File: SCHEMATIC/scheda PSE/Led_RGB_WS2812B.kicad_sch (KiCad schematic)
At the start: 16 parts

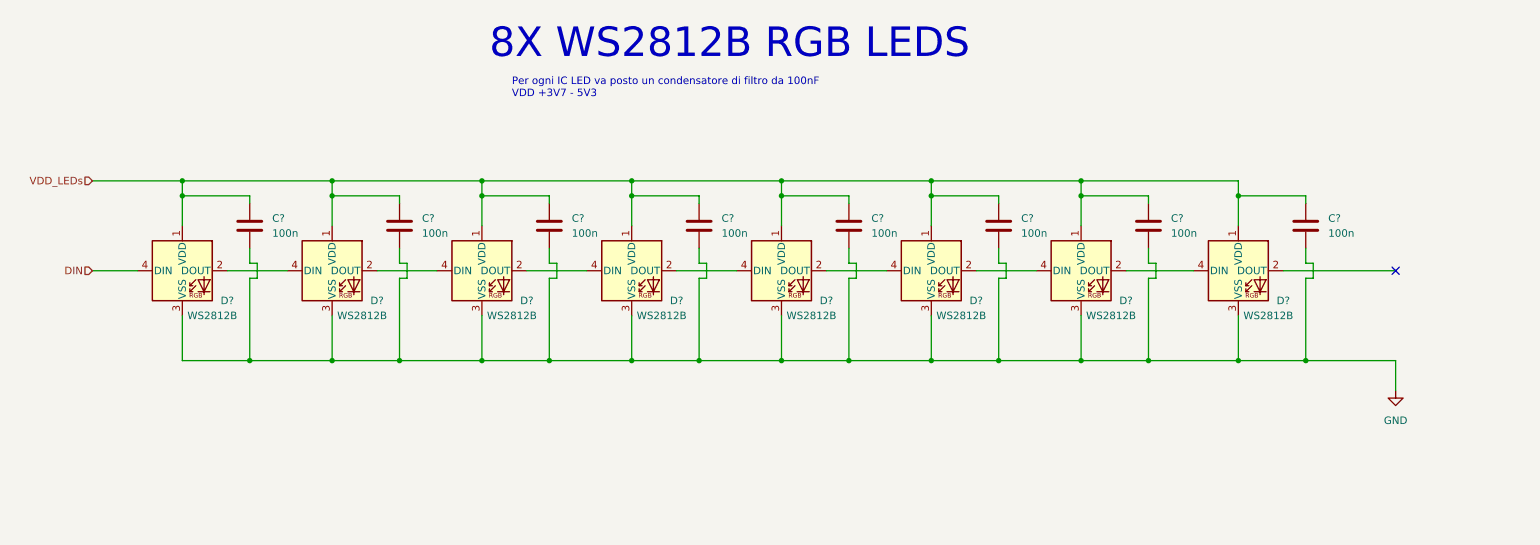
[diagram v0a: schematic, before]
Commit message: Sistemato tutto lo schematico con fogli gerarchici
Sistemato lo schematico, ordinato tutti i componenti nei vari fogli gerarchici.
aggiunto ldo e sistemato il buck converter. aggiunti anche i terminali a vite per le connessioni esterne
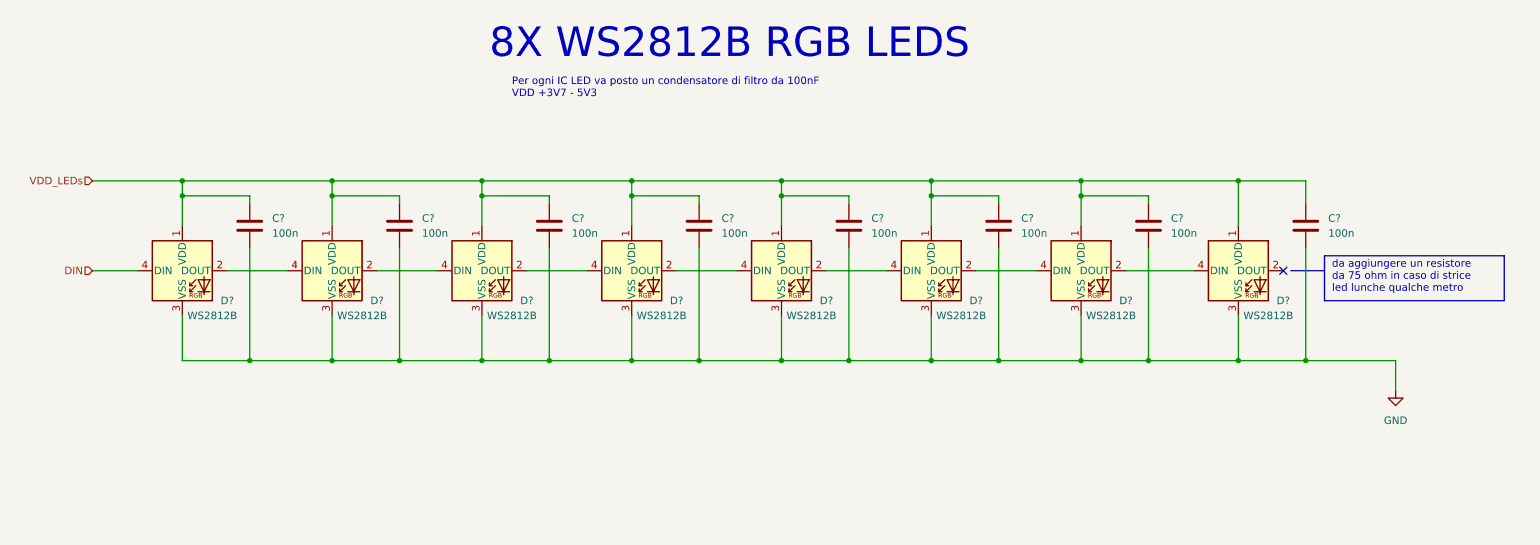
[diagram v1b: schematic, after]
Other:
- note added: "da aggiungere un resistore da 75 ohm in caso di strice led lunche qualche metro"
- title: (none) -> Scheda PSE RP2040

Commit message: sistemato tutto, e aggiunti i footprint da modificare
sistemato tutto, aggiunto e modificato i footprint.
Manca solo aggiungere i restanti footprint (praticamente solo dei componenti comuni)
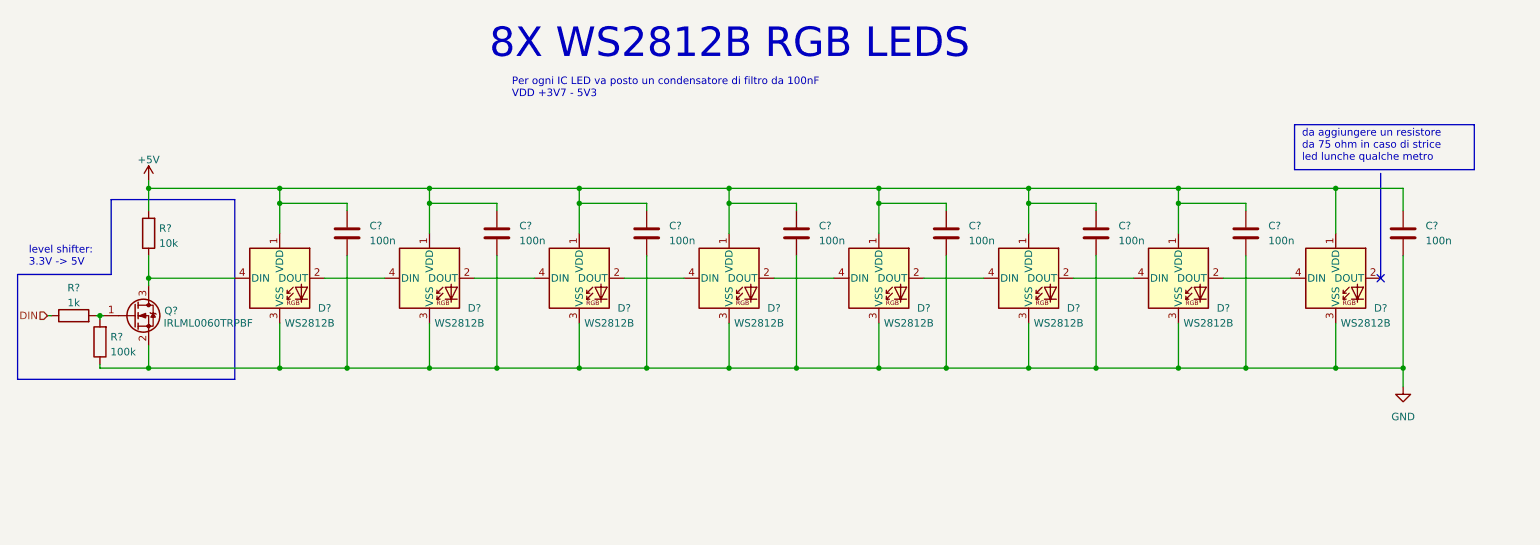
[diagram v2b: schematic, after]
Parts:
- added Q?: IRLML0060TRPBF, Package_TO_SOT_SMD:SOT-23, symbol Transistor_FET:IRLML2060
- added R?: 100k, symbol Device:R
- added R?: 10k, symbol Device:R
- added R?: 1k, symbol Device:R
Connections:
- net DIN: now also R?.1; no longer D?.4 (DIN)
- net GND: now also Q?.2 (S), R?.1
- net VDD_LEDs renamed +5V
- net +5V: now also R?.2
- new net: Q?.1 (G), R?.2, R?.2
- new net: D?.4 (DIN), Q?.3 (D), R?.1
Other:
- note added: "level shifter: 3.3V -> 5V"
- moved on the sheet: C?, D?

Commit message: Aggiunti QUASI tutti i footprint
aggiunti quasi tutti i footprint dei componenti
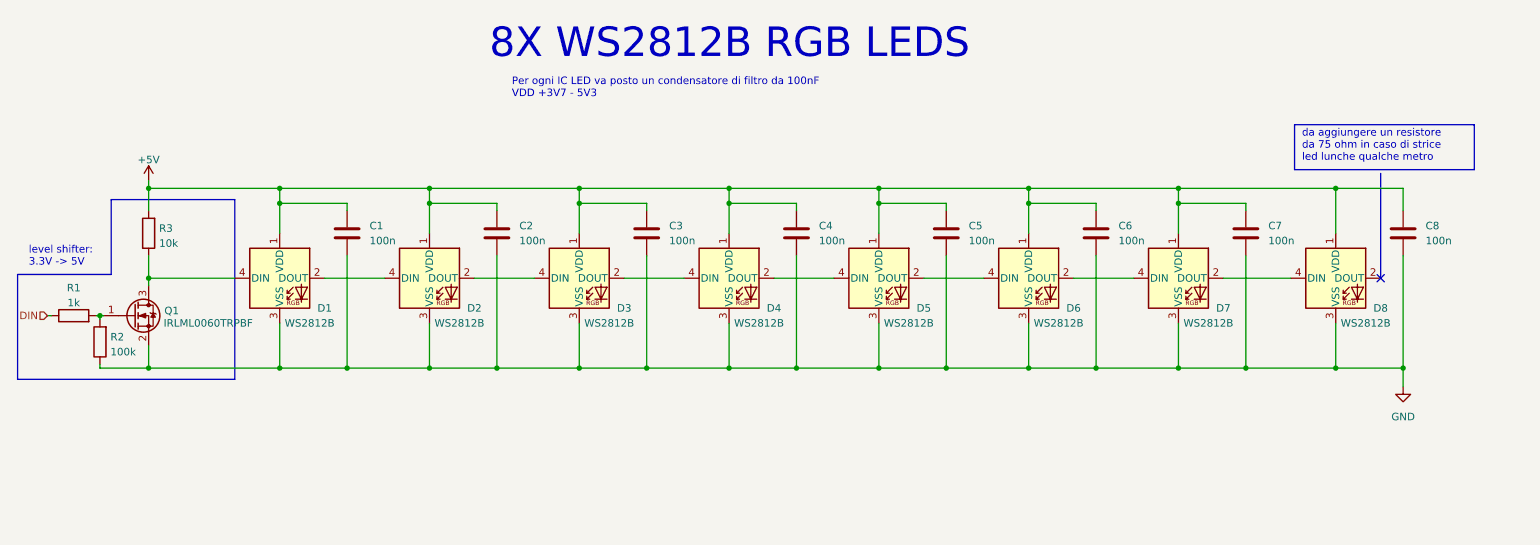
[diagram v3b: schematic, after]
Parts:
- C1, C2, C3, C4, C5, C6, C7, C8: renamed from C?; footprint (none) -> Capacitor_SMD:C_0603_1608Metric
- R1, R2, R3: renamed from R?; footprint (none) -> Resistor_SMD:R_0603_1608Metric
- gave numbers to parts that had none: 9

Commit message: Aggiunte tutte le cose richieste dal prof
Aggiunte tutte le cose richieste dal prof:
wifi
servo
uscita led
MANCA DA METERE IL SOLDER MASK SUI PAD NON USATI DEL GPS
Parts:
- added J1: WS2812B, Connector_JST:JST_XH_B3B-XH-A_1x03_P2.50mm_Vertical, symbol Connector_Generic:Conn_01x03
- added JP1: EXT_LEDs, Connector_PinHeader_2.54mm:PinHeader_1x02_P2.54mm_Vertical, symbol Jumper:Jumper_2_Open
- R3: value 10k -> 1k
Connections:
- net +5V: now also J1.2 (Pin_2)
- net DIN: now also Q1.3 (D), R3.1, J1.1 (Pin_1), JP1.1 (A)
- net GND: now also J1.3 (Pin_3)
- new net: D1.4 (DIN), JP1.2 (B)
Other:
- note added: "Connettore per striscia led esterna"
- note added: "da aggiungere un resistore da 75 ohm in caso di strice led lunghe qualche metro"
- note removed: "da aggiungere un resistore da 75 ohm in caso di strice led lunche qualche metro"
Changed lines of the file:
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@@
   (title_block
     (title "Scheda PSE RP2040")
-    (date "2023-03-29")
+    (date "2023-04-04")
     (rev "1.0")
     (comment 1 "Filippo Castellan ")
@@
   (junction (at 199.39 86.36) (diameter 0) (color 0 0 0 0)
   )
+  (junction (at 50.165 99.06) (diameter 0) (color 0 0 0 0)
+  )
   (junction (at 173.99 114.3) (diameter 0) (color 0 0 0 0)
   )
@@
   )
   (junction (at 173.99 83.82) (diameter 0) (color 0 0 0 0)
-  )
-  (junction (at 50.165 99.06) (diameter 0) (color 0 0 0 0)
   )
   (junction (at 224.79 86.36) (diameter 0) (color 0 0 0 0)
@@
     (stroke (width 0) (type default) (color 0 0 0 0))
   )
+  (wire (pts (xy 52.705 99.06) (xy 50.165 99.06))
+    (stroke (width 0) (type default) (color 0 0 0 0))
+  )
   (wire (pts (xy 123.19 83.82) (xy 148.59 83.82))
     (stroke (width 0) (type default) (color 0 0 0 0))
@@
     (stroke (width 0) (type default) (color 0 0 0 0))
   )
+  (wire (pts (xy 43.18 128.905) (xy 43.18 132.08))
+    (stroke (width 0) (type default) (color 0 0 0 0))
+  )
   (wire (pts (xy 224.79 86.36) (xy 224.79 91.44))
     (stroke (width 0) (type default) (color 0 0 0 0))
@@
     (stroke (width 0) (type default) (color 0 0 0 0))
   )
-  (wire (pts (xy 50.165 99.06) (xy 50.165 95.25))
+  (wire (pts (xy 50.165 95.25) (xy 50.165 99.06))
     (stroke (width 0) (type default) (color 0 0 0 0))
   )
@@
     (stroke (width 0) (type default) (color 0 0 0 0))
   )
+  (wire (pts (xy 43.18 132.08) (xy 50.165 132.08))
+    (stroke (width 0) (type default) (color 0 0 0 0))
+  )
   (wire (pts (xy 83.82 114.3) (xy 97.79 114.3))
     (stroke (width 0) (type default) (color 0 0 0 0))
@@
     (stroke (width 0) (type default) (color 0 0 0 0))
   )
+  (wire (pts (xy 43.18 134.62) (xy 43.18 136.525))
+    (stroke (width 0) (type default) (color 0 0 0 0))
+  )
   (wire (pts (xy 109.22 114.3) (xy 123.19 114.3))
     (stroke (width 0) (type default) (color 0 0 0 0))
@@
     (stroke (width 0) (type default) (color 0 0 0 0))
   )
+  (wire (pts (xy 62.865 99.06) (xy 64.77 99.06))
+    (stroke (width 0) (type default) (color 0 0 0 0))
+  )
   (wire (pts (xy 224.79 83.82) (xy 251.46 83.82))
     (stroke (width 0) (type default) (color 0 0 0 0))
@@
     (stroke (width 0) (type default) (color 0 0 0 0))
   )
+  (wire (pts (xy 50.165 134.62) (xy 43.18 134.62))
+    (stroke (width 0) (type default) (color 0 0 0 0))
+  )
   (polyline (pts (xy 274.955 80.645) (xy 244.475 80.645))
     (stroke (width 0) (type default) (color 0 0 0 0))
@@
     (stroke (width 0) (type default) (color 0 0 0 0))
   )
+  (wire (pts (xy 45.085 129.54) (xy 50.165 129.54))
+    (stroke (width 0) (type default) (color 0 0 0 0))
+  )
   (wire (pts (xy 123.19 114.3) (xy 134.62 114.3))
     (stroke (width 0) (type default) (color 0 0 0 0))
@@
     (stroke (width 0) (type default) (color 0 0 0 0))
   )
-  (wire (pts (xy 64.77 99.06) (xy 50.165 99.06))
-    (stroke (width 0) (type default) (color 0 0 0 0))
-  )
   (wire (pts (xy 148.59 114.3) (xy 160.02 114.3))
     (stroke (width 0) (type default) (color 0 0 0 0))
@@
     (stroke (width 0) (type default) (color 0 0 0 0))
   )
+  (wire (pts (xy 224.79 114.3) (xy 224.79 106.68))
+    (stroke (width 0) (type default) (color 0 0 0 0))
+  )
+  (wire (pts (xy 41.91 113.665) (xy 41.91 114.3))
+    (stroke (width 0) (type default) (color 0 0 0 0))
+  )
   (wire (pts (xy 50.165 99.06) (xy 50.165 100.33))
-    (stroke (width 0) (type default) (color 0 0 0 0))
-  )
-  (wire (pts (xy 224.79 114.3) (xy 224.79 106.68))
-    (stroke (width 0) (type default) (color 0 0 0 0))
-  )
-  (wire (pts (xy 41.91 113.665) (xy 41.91 114.3))
     (stroke (width 0) (type default) (color 0 0 0 0))
   )
@@
     (effects (font (size 1.27 1.27)) (justify left bottom))
   )
-  (text "da aggiungere un resistore\nda 75 ohm in caso di strice\nled lunche qualche metro"
+  (text "Connettore per striscia\nled esterna" (at 58.42 134.62 0)
+    (effects (font (size 1.27 1.27)) (justify left bottom))
+  )
+  (text "da aggiungere un resistore\nda 75 ohm in caso di strice\nled lunghe qualche metro"
     (at 245.745 79.375 0)
     (effects (font (size 1.27 1.27)) (justify left bottom))
@@
   (text "8X WS2812B RGB LEDS\n" (at 107.95 62.23 0)
     (effects (font (size 5 5)) (justify left bottom))
+  )
+  (label "DIN" (at 45.085 129.54 0)
+    (effects (font (size 1.27 1.27)) (justify left bottom))
+  )
+  (label "DIN" (at 50.165 99.06 0)
+    (effects (font (size 1.27 1.27)) (justify left bottom))
   )
   (hierarchical_label "DIN" (shape input) (at 33.02 105.41 180)
@@
   (symbol (lib_id "power:+5V") (at 50.165 82.55 0) (unit 1)
     (in_bom yes) (on_board yes) (fields_autoplaced)
-    (property "Reference" "#PWR01" (id 0) (at 50.165 86.36 0)
+    (property "Reference" "#PWR03" (id 0) (at 50.165 86.36 0)
       (effects (font (size 1.27 1.27)) hide)
     )
@@
   (symbol (lib_id "power:GND") (at 262.89 117.475 0) (unit 1)
     (in_bom yes) (on_board yes) (fields_autoplaced)
-    (property "Reference" "#PWR02" (id 0) (at 262.89 123.825 0)
+    (property "Reference" "#PWR04" (id 0) (at 262.89 123.825 0)
       (effects (font (size 1.27 1.27)) hide)
     )
@@
       (effects (font (size 1.27 1.27)) (justify right))
     )
-    (property "Value" "10k" (id 1) (at 51.943 93.1422 0)
+    (property "Value" "1k" (id 1) (at 51.943 93.1422 0)
       (effects (font (size 1.27 1.27)) (justify right))
     )
@@
     (pin "1")
     (pin "2")
+  )
+  (symbol (lib_id "power:GND") (at 43.18 136.525 0) (unit 1)
+    (in_bom yes) (on_board yes) (fields_autoplaced)
+    (property "Reference" "#PWR02" (id 0) (at 43.18 142.875 0)
+      (effects (font (size 1.27 1.27)) hide)
+    )
+    (property "Value" "GND" (id 1) (at 43.18 140.9684 0))
+    (property "Footprint" "" (id 2) (at 43.18 136.525 0)
+      (effects (font (size 1.27 1.27)) hide)
+    )
+    (property "Datasheet" "" (id 3) (at 43.18 136.525 0)
+      (effects (font (size 1.27 1.27)) hide)
+    )
+    (pin "1")
   )
   (symbol (lib_id "LED:WS2812B") (at 199.39 99.06 0) (unit 1)
@@
     (pin "4")
   )
+  (symbol (lib_id "Connector_Generic:Conn_01x03") (at 55.245 132.08 0) (unit 1)
+    (in_bom yes) (on_board yes)
+    (property "Reference" "J1" (id 0) (at 53.975 124.46 0)
+      (effects (font (size 1.27 1.27)) (justify left))
+    )
+    (property "Value" "WS2812B" (id 1) (at 50.8 127 0)
+      (effects (font (size 1.27 1.27)) (justify left))
+    )
+    (property "Footprint" "Connector_JST:JST_XH_B3B-XH-A_1x03_P2.50mm_Vertical" (id 2) (at 55.245 132.08 0)
+      (effects (font (size 1.27 1.27)) hide)
+    )
+    (property "Datasheet" "~" (id 3) (at 55.245 132.08 0)
+      (effects (font (size 1.27 1.27)) hide)
+    )
+    (pin "1")
+    (pin "2")
+    (pin "3")
+  )
   (symbol (lib_id "LED:WS2812B") (at 251.46 99.06 0) (unit 1)
     (in_bom yes) (on_board yes)
@@
       (effects (font (size 1.27 1.27)) hide)
     )
+    (pin "1")
+    (pin "2")
+  )
+  (symbol (lib_id "power:+5V") (at 43.18 128.905 0) (unit 1)
+    (in_bom yes) (on_board yes) (fields_autoplaced)
+    (property "Reference" "#PWR01" (id 0) (at 43.18 132.715 0)
+      (effects (font (size 1.27 1.27)) hide)
+    )
+    (property "Value" "+5V" (id 1) (at 43.18 125.3292 0))
+    (property "Footprint" "" (id 2) (at 43.18 128.905 0)
+      (effects (font (size 1.27 1.27)) hide)
+    )
+    (property "Datasheet" "" (id 3) (at 43.18 128.905 0)
+      (effects (font (size 1.27 1.27)) hide)
+    )
+    (pin "1")
+  )
+  (symbol (lib_id "Jumper:Jumper_2_Open") (at 57.785 99.06 0) (unit 1)
+    (in_bom yes) (on_board yes) (fields_autoplaced)
+    (property "Reference" "JP1" (id 0) (at 57.785 93.7092 0))
+    (property "Value" "EXT_LEDs" (id 1) (at 57.785 96.2461 0))
+    (property "Footprint" "Connector_PinHeader_2.54mm:PinHeader_1x02_P2.54mm_Vertical" (id 2) (at 57.785 99.06 0)
+      (effects (font (size 1.27 1.27)) hide)
+    )
+    (property "Datasheet" "~" (id 3) (at 57.785 99.06 0)
+      (effects (font (size 1.27 1.27)) hide)
+    )

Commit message: Versione definitiva inviata ai prof
Sistemato tutto e inviato il tutto ai prof
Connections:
- net DIN: no longer J1.1 (Pin_1), JP1.1 (A), Q1.3 (D), R3.1
- new net DIN_INT: J1.1 (Pin_1), JP1.1 (A), Q1.3 (D), R3.1
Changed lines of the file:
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@@
     (stroke (width 0) (type default) (color 0 0 0 0))
   )
-  (wire (pts (xy 43.18 128.905) (xy 43.18 132.08))
+  (wire (pts (xy 40.005 128.905) (xy 40.005 132.08))
     (stroke (width 0) (type default) (color 0 0 0 0))
   )
@@
     (stroke (width 0) (type default) (color 0 0 0 0))
   )
-  (wire (pts (xy 43.18 132.08) (xy 50.165 132.08))
+  (wire (pts (xy 40.005 132.08) (xy 50.165 132.08))
     (stroke (width 0) (type default) (color 0 0 0 0))
   )
@@
     (stroke (width 0) (type default) (color 0 0 0 0))
   )
-  (wire (pts (xy 43.18 134.62) (xy 43.18 136.525))
+  (wire (pts (xy 40.005 134.62) (xy 40.005 136.525))
     (stroke (width 0) (type default) (color 0 0 0 0))
   )
@@
     (stroke (width 0) (type default) (color 0 0 0 0))
   )
-  (polyline (pts (xy 43.815 85.725) (xy 43.815 98.425))
+  (polyline (pts (xy 42.545 85.725) (xy 42.545 98.425))
     (stroke (width 0) (type default) (color 0 0 0 0))
   )
@@
     (stroke (width 0) (type default) (color 0 0 0 0))
   )
-  (polyline (pts (xy 43.815 98.425) (xy 27.94 98.425))
+  (polyline (pts (xy 42.545 98.425) (xy 27.94 98.425))
     (stroke (width 0) (type default) (color 0 0 0 0))
   )
@@
     (stroke (width 0) (type default) (color 0 0 0 0))
   )
-  (wire (pts (xy 50.165 134.62) (xy 43.18 134.62))
+  (wire (pts (xy 50.165 134.62) (xy 40.005 134.62))
     (stroke (width 0) (type default) (color 0 0 0 0))
   )
@@
     (stroke (width 0) (type default) (color 0 0 0 0))
   )
-  (wire (pts (xy 45.085 129.54) (xy 50.165 129.54))
-    (stroke (width 0) (type default) (color 0 0 0 0))
-  )
   (wire (pts (xy 123.19 114.3) (xy 134.62 114.3))
     (stroke (width 0) (type default) (color 0 0 0 0))
@@
     (stroke (width 0) (type default) (color 0 0 0 0))
   )
+  (wire (pts (xy 42.545 129.54) (xy 50.165 129.54))
+    (stroke (width 0) (type default) (color 0 0 0 0))
+  )
   (wire (pts (xy 224.79 114.3) (xy 224.79 106.68))
     (stroke (width 0) (type default) (color 0 0 0 0))
@@
     (stroke (width 0) (type default) (color 0 0 0 0))
   )
-  (polyline (pts (xy 43.815 85.725) (xy 64.77 85.725))
+  (polyline (pts (xy 42.545 85.725) (xy 64.77 85.725))
     (stroke (width 0) (type default) (color 0 0 0 0))
   )
@@
     (effects (font (size 5 5)) (justify left bottom))
   )
-  (label "DIN" (at 45.085 129.54 0)
-    (effects (font (size 1.27 1.27)) (justify left bottom))
-  )
-  (label "DIN" (at 50.165 99.06 0)
+  (label "DIN_INT" (at 50.165 97.79 180)
+    (effects (font (size 1.27 1.27)) (justify right bottom))
+  )
+  (label "DIN_INT" (at 42.545 129.54 0)
     (effects (font (size 1.27 1.27)) (justify left bottom))
   )
@@
     (pin "2")
   )
-  (symbol (lib_id "power:GND") (at 43.18 136.525 0) (unit 1)
-    (in_bom yes) (on_board yes) (fields_autoplaced)
-    (property "Reference" "#PWR02" (id 0) (at 43.18 142.875 0)
-      (effects (font (size 1.27 1.27)) hide)
-    )
-    (property "Value" "GND" (id 1) (at 43.18 140.9684 0))
-    (property "Footprint" "" (id 2) (at 43.18 136.525 0)
-      (effects (font (size 1.27 1.27)) hide)
-    )
-    (property "Datasheet" "" (id 3) (at 43.18 136.525 0)
+  (symbol (lib_id "power:GND") (at 40.005 136.525 0) (unit 1)
+    (in_bom yes) (on_board yes) (fields_autoplaced)
+    (property "Reference" "#PWR02" (id 0) (at 40.005 142.875 0)
+      (effects (font (size 1.27 1.27)) hide)
+    )
+    (property "Value" "GND" (id 1) (at 40.005 140.9684 0))
+    (property "Footprint" "" (id 2) (at 40.005 136.525 0)
+      (effects (font (size 1.27 1.27)) hide)
+    )
+    (property "Datasheet" "" (id 3) (at 40.005 136.525 0)
       (effects (font (size 1.27 1.27)) hide)
     )
@@
     (pin "2")
   )
-  (symbol (lib_id "power:+5V") (at 43.18 128.905 0) (unit 1)
-    (in_bom yes) (on_board yes) (fields_autoplaced)
-    (property "Reference" "#PWR01" (id 0) (at 43.18 132.715 0)
-      (effects (font (size 1.27 1.27)) hide)
-    )
-    (property "Value" "+5V" (id 1) (at 43.18 125.3292 0))
-    (property "Footprint" "" (id 2) (at 43.18 128.905 0)
-      (effects (font (size 1.27 1.27)) hide)
-    )
-    (property "Datasheet" "" (id 3) (at 43.18 128.905 0)
-      (effects (font (size 1.27 1.27)) hide)
-    )
+  (symbol (lib_id "power:+5V") (at 40.005 128.905 0) (unit 1)
+    (in_bom yes) (on_board yes)
+    (property "Reference" "#PWR01" (id 0) (at 40.005 132.715 0)
+      (effects (font (size 1.27 1.27)) hide)
+    )
+    (property "Value" "+5V" (id 1) (at 40.005 125.095 0))
+    (property "Footprint" "" (id 2) (at 40.005 128.905 0)
+      (effects (font (size 1.27 1.27)) hide)
+    )
+    (property "Datasheet" "" (id 3) (at 40.005 128.905 0)
+      (effects (font (size 1.27 1.27)) hide)
+    )
